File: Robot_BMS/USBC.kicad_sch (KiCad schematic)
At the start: 9 parts, among them IC1 STUSB4710AQTR, J1 632723300011

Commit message: all symbols footprints & models added
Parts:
- C4: renamed from C6; footprint CAP_1608_TDK -> RobotBMS:CAP_1608_TDK
- C5: renamed from C4; footprint CAP_1608_TDK -> RobotBMS:CAP_1608_TDK
- C6: renamed from C3; footprint CAPC1608X90N -> RobotBMS:CAPC1608X90N
- R6: renamed from R5; footprint RES_R0603_ROM -> RobotBMS:RES_R0603_ROM
- R7: renamed from R6; footprint RES_V0603_VIS -> RobotBMS:RES_V0603_VIS
- R8: renamed from R7; footprint AT0603DRE07100RL:RESC1608X55N -> RobotBMS:RESC1608X55N
- renumbered TP1 to TP7
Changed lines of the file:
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@@
 		(dnp no)
 		(fields_autoplaced yes)
-		(property "Reference" "R5"
+		(property "Reference" "R6"
 			(at 54.102 126.9999 90)
 			(effects
@@
 			)
 		)
-		(property "Footprint" "RES_R0603_ROM"
+		(property "Footprint" "RobotBMS:RES_R0603_ROM"
 			(at 52.07 134.62 0)
 			(effects
@@
 			(project "Robot_BMS"
 				(path "/72551b1c-3d40-4199-8911-e5b015f4abec/c1bdabe1-a4b5-470d-80f8-90d5658c2a45"
-					(reference "R5")
+					(reference "R6")
 					(unit 1)
 				)
@@
 		(dnp no)
 		(fields_autoplaced yes)
-		(property "Reference" "R6"
+		(property "Reference" "R7"
 			(at 215.392 24.6379 90)
 			(effects
@@
 			)
 		)
-		(property "Footprint" "RES_V0603_VIS"
+		(property "Footprint" "RobotBMS:RES_V0603_VIS"
 			(at 213.106 19.558 0)
 			(effects
@@
 			(project ""
 				(path "/72551b1c-3d40-4199-8911-e5b015f4abec/c1bdabe1-a4b5-470d-80f8-90d5658c2a45"
-					(reference "R6")
+					(reference "R7")
 					(unit 1)
 				)
@@
 		(dnp no)
 		(fields_autoplaced yes)
-		(property "Reference" "C3"
+		(property "Reference" "C6"
 			(at 259.842 35.8139 90)
 			(effects
@@
 			)
 		)
-		(property "Footprint" "CAPC1608X90N"
+		(property "Footprint" "RobotBMS:CAPC1608X90N"
 			(at 352.222 34.544 0)
 			(effects
@@
 			(project "Robot_BMS"
 				(path "/72551b1c-3d40-4199-8911-e5b015f4abec/c1bdabe1-a4b5-470d-80f8-90d5658c2a45"
-					(reference "C3")
+					(reference "C6")
 					(unit 1)
 				)
@@
 		(dnp no)
 		(fields_autoplaced yes)
-		(property "Reference" "C6"
+		(property "Reference" "C4"
 			(at 104.14 74.9299 90)
 			(effects
@@
 			)
 		)
-		(property "Footprint" "CAP_1608_TDK"
+		(property "Footprint" "RobotBMS:CAP_1608_TDK"
 			(at 100.838 72.39 0)
 			(effects
@@
 			(project ""
 				(path "/72551b1c-3d40-4199-8911-e5b015f4abec/c1bdabe1-a4b5-470d-80f8-90d5658c2a45"
-					(reference "C6")
+					(reference "C4")
 					(unit 1)
 				)
@@
 		(dnp no)
 		(fields_autoplaced yes)
-		(property "Reference" "C4"
+		(property "Reference" "C5"
 			(at 115.824 74.9299 90)
 			(effects
@@
 			)
 		)
-		(property "Footprint" "CAP_1608_TDK"
+		(property "Footprint" "RobotBMS:CAP_1608_TDK"
 			(at 112.522 72.39 0)
 			(effects
@@
 			(project "Robot_BMS"
 				(path "/72551b1c-3d40-4199-8911-e5b015f4abec/c1bdabe1-a4b5-470d-80f8-90d5658c2a45"
-					(reference "C4")
+					(reference "C5")
 					(unit 1)
 				)
@@
 		(dnp no)
 		(fields_autoplaced yes)
-		(property "Reference" "TP1"
+		(property "Reference" "TP7"
 			(at 271.526 22.3519 0)
 			(effects
@@
 			(project ""
 				(path "/72551b1c-3d40-4199-8911-e5b015f4abec/c1bdabe1-a4b5-470d-80f8-90d5658c2a45"
-					(reference "TP1")
+					(reference "TP7")
 					(unit 1)
 				)
@@
 		(dnp no)
 		(fields_autoplaced yes)
-		(property "Reference" "R7"
+		(property "Reference" "R8"
 			(at 235.204 151.892 0)
 			(effects
@@
 			)
 		)
-		(property "Footprint" "AT0603DRE07100RL:RESC1608X55N"
+		(property "Footprint" "RobotBMS:RESC1608X55N"
 			(at 235.204 159.004 0)
 			(effects
@@
 			(project ""
 				(path "/72551b1c-3d40-4199-8911-e5b015f4abec/c1bdabe1-a4b5-470d-80f8-90d5658c2a45"
-					(reference "R7")
-					(unit 1)
-				)
+					(reference "R8")
+					(unit 1)
+				)

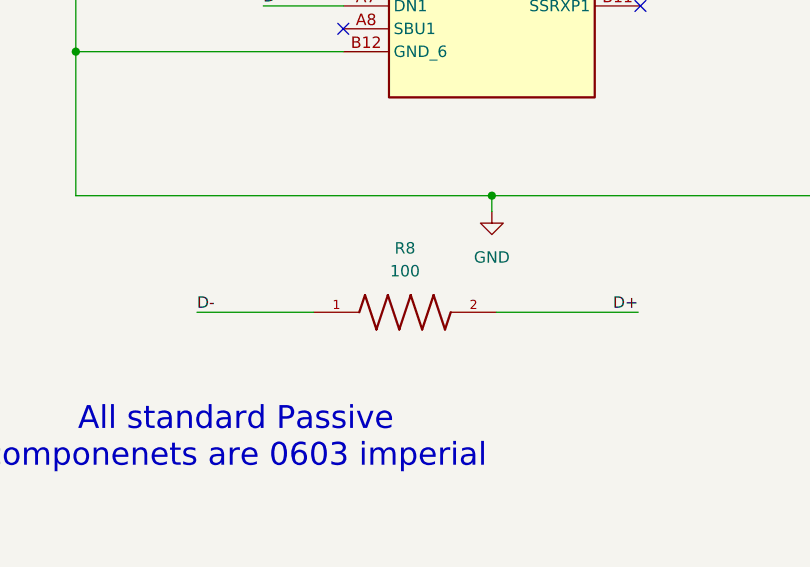
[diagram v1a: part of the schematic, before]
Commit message: BOM done, with total price £40
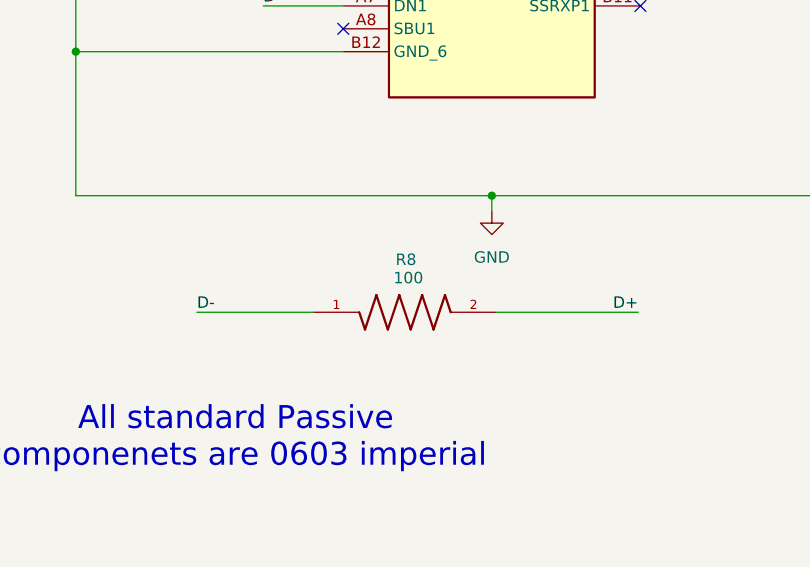
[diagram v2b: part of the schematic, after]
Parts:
- C4, C5: Manufacturer_Part_Number (none) -> C1608X5R1H105K080AB; Price (none) -> 0.156
- C6: Price (none) -> 0.11
- IC1: Price (none) -> 1.03
- J1: Price (none) -> 3.62
- R6: Manufacturer_Part_Number (none) -> ESR03EZPF1003; Price (none) -> 0.12
- R7: Manufacturer_Part_Number (none) -> CRCW06031K00JNEAIF; Price (none) -> 0.336
- R8: Manufacturer_Part_Number (none) -> AT0603DRE07100RL; Price None -> 0.068
- TP7: Manufacturer_Part_Number (none) -> exposed pad; Price (none) -> 0

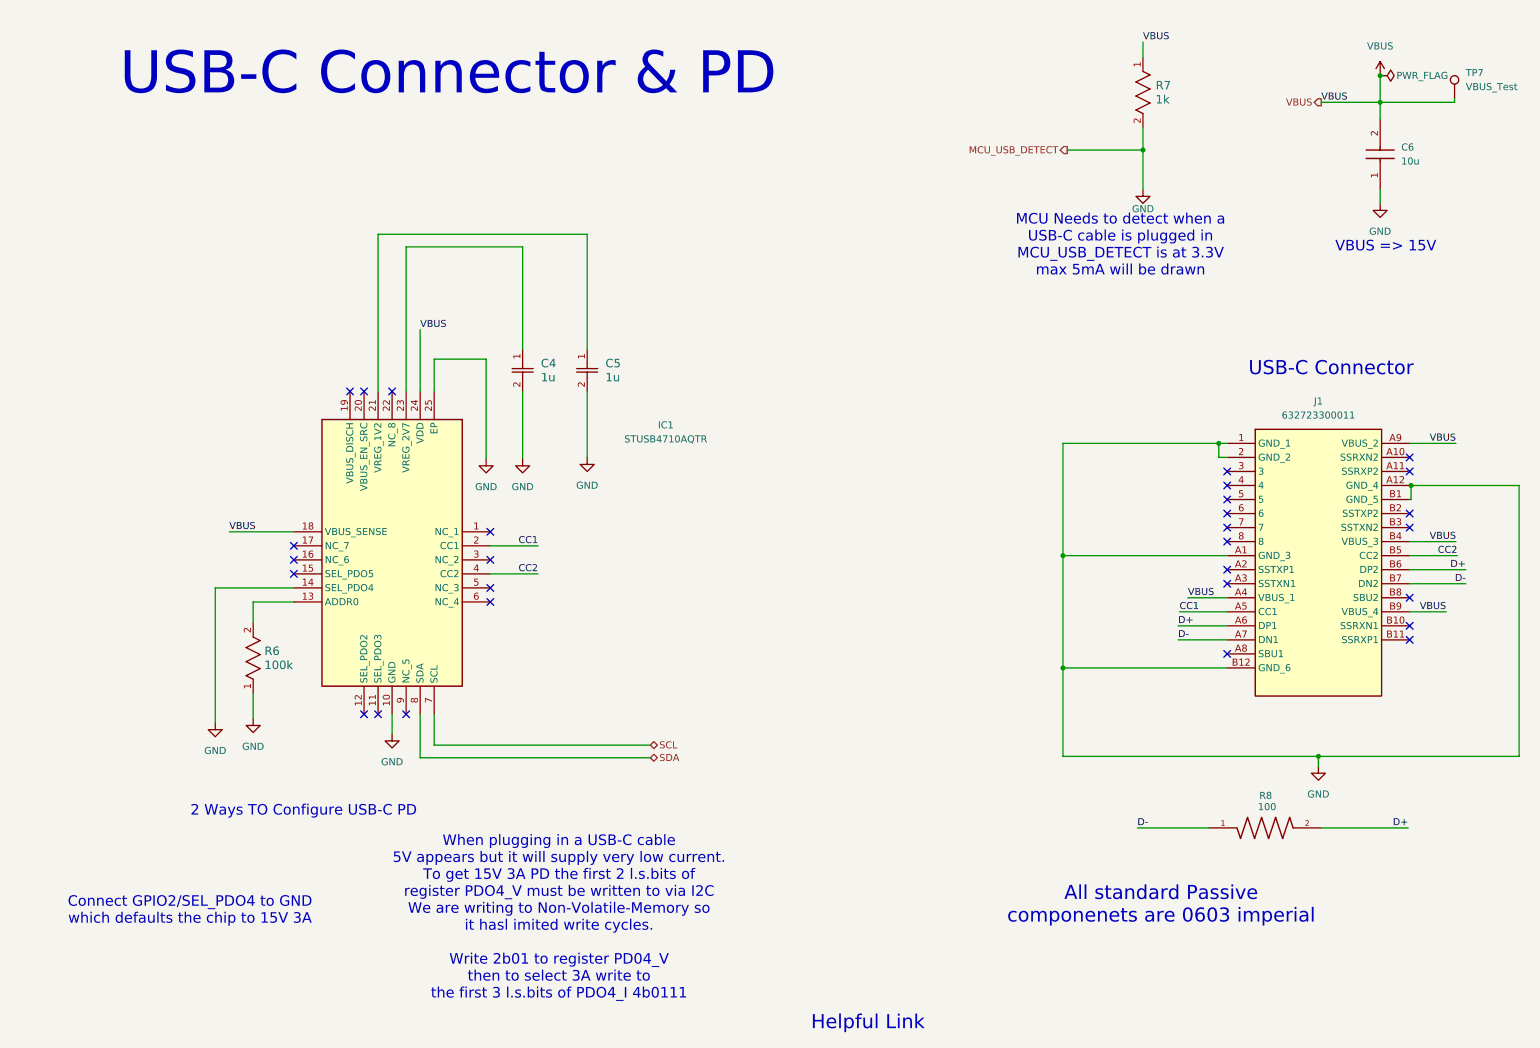
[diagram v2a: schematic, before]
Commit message: switching usb c pd chip to ap33772 due to better support online
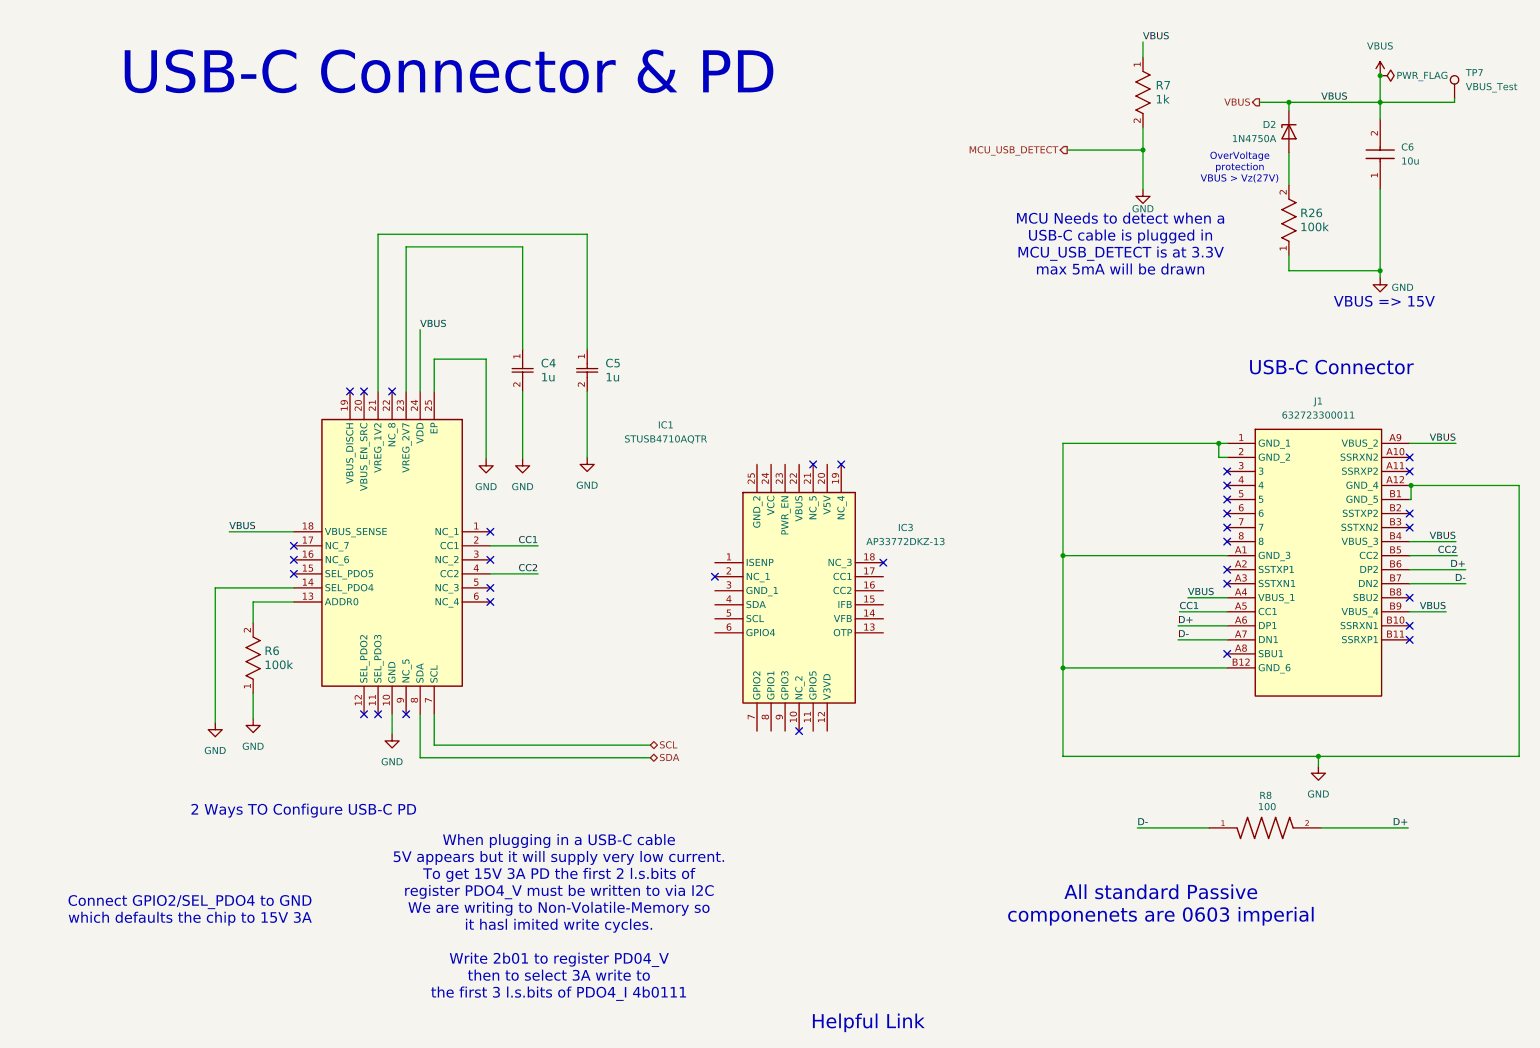
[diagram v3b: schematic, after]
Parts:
- added D2: 1N4750A, Diode_THT:D_DO-41_SOD81_P10.16mm_Horizontal, symbol Diode:1N47xxA
- added IC3: AP33772DKZ-13, QFN50P400X400X80-25N-D, symbol AP33772DKZ-13:AP33772DKZ-13
- added R26: 100k, RobotBMS:RES_R0603_ROM, symbol ESR03EZPF1003:ESR03EZPF1003
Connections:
- net GND: now also R26.1
- net VBUS: now also D2.1 (K)
- new net: D2.2 (A), R26.2
- no-connect marks 29 -> 34
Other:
- note added: "OverVoltage protection VBUS > Vz(27V)"

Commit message: mid way implementing new usb-pd chip
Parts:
- removed C5: 1u, RobotBMS:CAP_1608_TDK, symbol C1608X5R1H105K080AB:C1608X5R1H105K080AB
- removed IC1: STUSB4710AQTR, RobotBMS:QFN50P400X400X100-25N-D, symbol STUSB4710AQTR:STUSB4710AQTR
- removed R6: 100k, RobotBMS:RES_R0603_ROM, symbol ESR03EZPF1003:ESR03EZPF1003
- added C25, C28: 0.1u, RobotBMS:CAPC17595_87N_KEM, symbol C0603C104K5RACAUTO:C0603C104K5RACAUTO
- added C26: 1u, RobotBMS:CAP_1608_TDK, symbol C1608X5R1H105K080AB:C1608X5R1H105K080AB
- added C27: 10u, RobotBMS:CAPC1608X90N, symbol CL10A106MA8NRNC:CL10A106MA8NRNC
- added Q5, Q6: NDT3055L, Package_TO_SOT_SMD:SOT-223-3_TabPin2, symbol Transistor_FET:NDT3055L
- added R29, R30: 5k1, ERA3AEB101V, symbol ERA-£AED512V:ERA-3AED512V
- added R31: 10 milli_ohm, RESC1608X60N, symbol UR73D1JTTD10L0F:UR73D1JTTD10L0F
- added R32: 1k, RobotBMS:RES_V0603_VIS, symbol CRCW06031K00JNEAIF:CRCW06031K00JNEAIF
- added RT1: 10k, THRMC0603X33N, symbol NCP03XH103F05RL:NCP03XH103F05RL
- IC3: Price (none) -> 2.22
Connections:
- net CC1: now also IC3.17 (CC1), R30.1
- net CC2: now also IC3.16 (CC2), R29.1
- net GND: now also IC3.25 (GND_2), IC3.3 (GND_1), C25.2, C26.2, C27.2, C28.2, R29.2, R30.2, RT1.2
- net SCL: now also IC3.5 (SCL)
- net SDA: now also IC3.4 (SDA)
- net VBUS: now also IC3.1 (ISENP), C27.1, R31.1
- net USB_C: now reaches C4.1
- net USB_C: now also IC3.22 (VBUS), Q6.3 (S)
- net at IC3.12 (V3VD): now also C28.1
- net at IC3.13 (OTP): now also RT1.1
- net at IC3.15 (IFB): now also C25.1
- net at IC3.20 (V5V): now also C26.1
- net at IC3.23 (PWR_EN): now also R32.2
- net VCC: now reaches IC3.24 (VCC)
- net VCC: now also Q5.2 (D), R31.2
- new net: Q5.1 (G), Q6.1 (G), R32.1
- new net: Q5.3 (S), Q6.2 (D)
- no-connect marks 34 -> 22
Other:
- moved on the sheet: IC3
